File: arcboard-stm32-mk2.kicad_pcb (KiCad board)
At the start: 2 copper layers, 60 x 60 mm, 88 parts, among them J1 Conn_01x04_Socket, J17 Conn_01x04_Socket, J2 Conn_01x04_Socket, J3 Conn_01x04_Socket, J5 Conn_01x02_Socket, J6 Conn_01x02_Socket, J7 Conn_01x02_Socket, U1 XC6210B332MR-G, U13 2N7002, U14 W25Q128JVSIQTR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

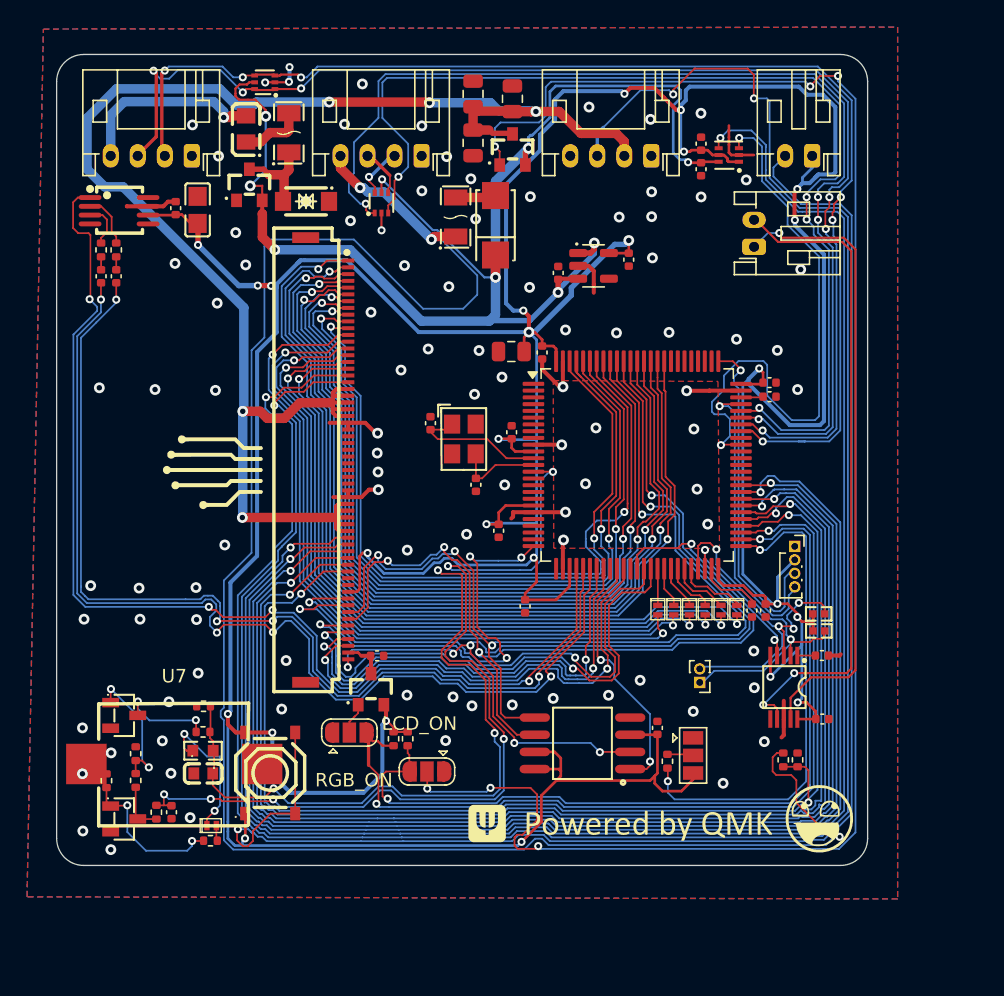
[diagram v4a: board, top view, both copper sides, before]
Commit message: re-organized the bottom section to fit a piezo
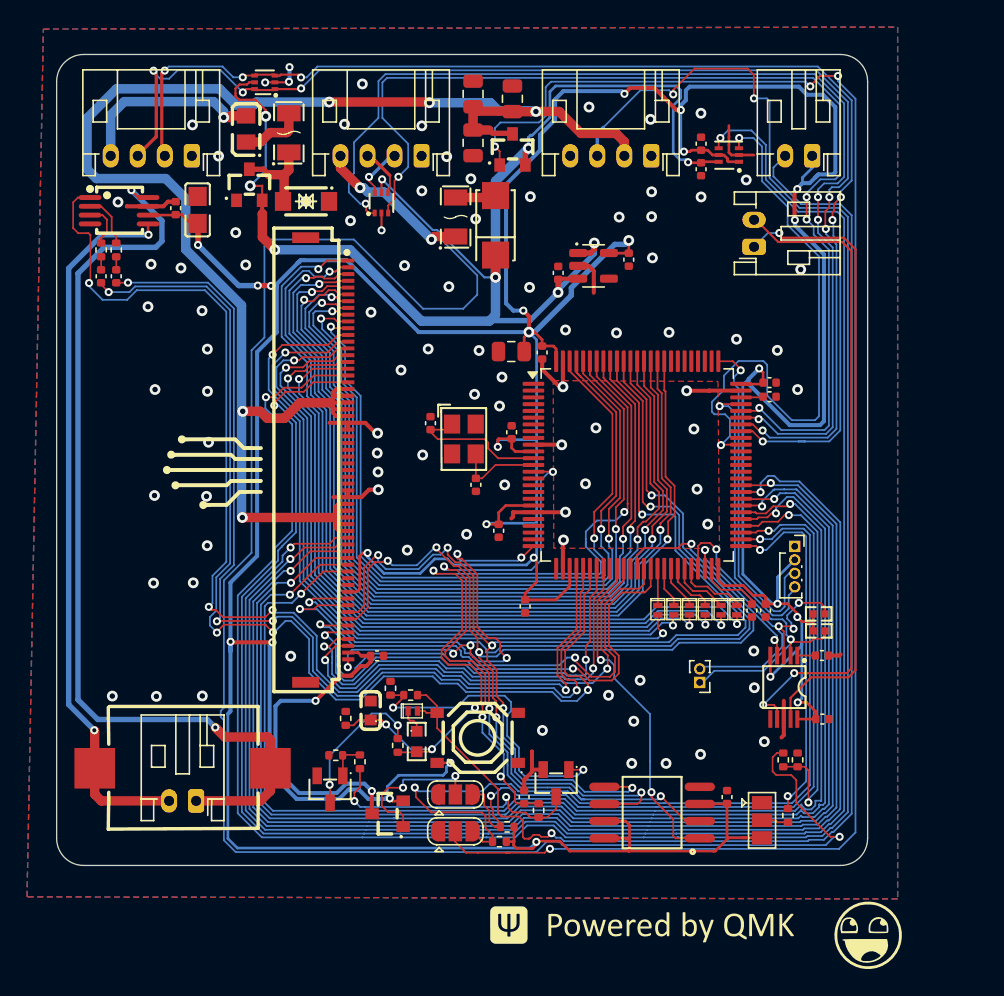
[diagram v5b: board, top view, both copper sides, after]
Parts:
- added J4: Conn_01x02_Socket, Connector_JST:JST_PH_S2B-PH-K_1x02_P2.00mm_Horizontal, F.Cu at (80.3, 125.2)
- moved U13 32.1 mm to (107.0, 123.9), turned to 90 degrees
- moved R14 28.3 mm to (105.7, 125.9)
- moved C17 26.1 mm to (104.6, 124.9), turned to -90 degrees
- moved R16 22.1 mm to (94.7, 116.9)
- moved R15 18.3 mm to (96.2, 117.4)
- moved D11 17.1 mm to (96.3, 118.6)
- moved R3 16.6 mm to (92.4, 122.3)
- moved U4 16.2 mm to (90.2, 124.4), turned to 90 degrees
- moved R6 15.8 mm to (96.6, 120.8), turned to -90 degrees
- moved U15 15.6 mm to (101.2, 120.6), turned to 180 degrees
- moved R9 14.8 mm to (90.7, 121.8), turned to 180 degrees
- moved R2 14.4 mm to (95.2, 121.1), turned to -90 degrees
- moved C22 13.2 mm to (93.2, 118.5), turned to 90 degrees
- moved R8 10.6 mm to (103.3, 127.2), turned to 180 degrees
- moved R1 10.6 mm to (91.4, 119.1), turned to 90 degrees
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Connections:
- U15 pad 1: +3V3 -> unconnected-(U15-A-Pad1)
- U15 pad 3: Net-(D11-A) -> unconnected-(U15-C-Pad3)
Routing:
- net VO-: track 0.00 -> 70.3 mm
- net VO+: track 0.00 -> 53.2 mm, vias 0 -> 2
- net NRST: track 65.4 -> 40.9 mm, vias 6 -> 4
- net LCD_3V3: track 3.09 -> 25.4 mm, vias 0 -> 2
- net BOOT0: track 82.2 -> 61.3 mm, vias 4 -> 5
- net Net-(D11-A): track 115.7 -> 95.2 mm
- net Net-(U13-D): track 3.87 -> 20.4 mm, vias 0 -> 2
- net SPI1_CLK: track 74.5 -> 89.6 mm, vias 4 -> 6
- net SPI1_MOSI: track 73.5 -> 87.4 mm, vias 4 -> 6
- net +3V3: track 371.8 -> 384.1 mm
- net Net-(U13-G): track 11.5 -> 23.3 mm
- net SPLIT_HAND: track 36.5 -> 26.5 mm
- net SPI1_MISO: track 75.4 -> 85.4 mm
- net LCD_ON: track 66.1 -> 56.5 mm
- net Net-(JP4-C): track 2.34 -> 11.2 mm, vias 0 -> 2
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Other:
- board text removed: "LCD_ON"
- board text removed: "RGB_ON"

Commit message: silkscreen work, adding lse crystal and vbat hookup
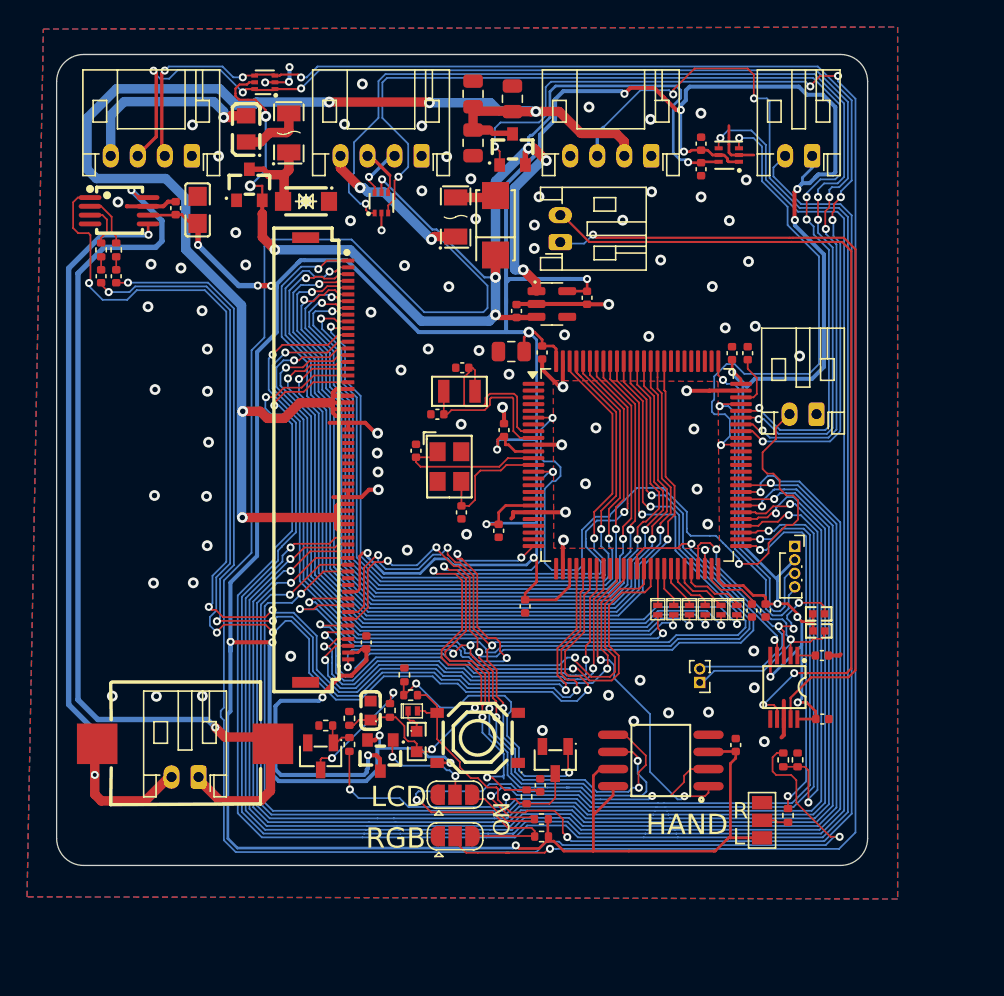
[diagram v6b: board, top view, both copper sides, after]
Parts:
- removed LOGO2: **REF, kicad-libraries:awesome-logo
- removed LOGO7: **REF, kicad-libraries:awesome-logo-25mm
- added C29: 12p, Capacitor_SMD:C_0402_1005Metric, F.Cu at (98.2, 96.6)
- added C30: 12p, Capacitor_SMD:C_0402_1005Metric, F.Cu at (100.0, 93.2)
- added J8: Conn_01x02_Socket, Connector_JST:JST_PH_S2B-PH-K_1x02_P2.00mm_Horizontal, F.Cu at (126.2, 96.6)
- added U8: SC-32S32_768kHz20PPM7pF, kicad-libraries:OSC-SMD_L3.2-W1.5, F.Cu at (99.8, 94.9)
- LOGO3, LOGO4: moved to B.Cu
- moved LOGO3 19.1 mm to (73.8, 83.2), turned to 180 degrees
- moved J7 14.3 mm to (107.3, 83.9)
- moved LOGO4 8.46 mm to (117.7, 127.2), turned to 180 degrees
- moved MOSFET3 4.33 mm to (94.0, 121.9), turned to 90 degrees
- moved C13 4.18 mm to (104.0, 89.0)
- moved C27 4.18 mm to (109.2, 88.0)
- moved U1 4.18 mm to (106.6, 88.5)
- moved U14 3.90 mm to (114.7, 122.2)
- moved C14 3.90 mm to (120.2, 121.1)
- moved C21 3.60 mm to (121.1, 92.1), turned to -90 degrees
- moved C7 3.53 mm to (120.0, 92.1), turned to -90 degrees
- moved R7 3.14 mm to (105.9, 127.9)
- moved R2 2.65 mm to (94.7, 118.5)
- moved R8 2.61 mm to (105.9, 126.6)
- moved U4 2.54 mm to (89.5, 121.9)
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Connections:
- U2 pad 6: unconnected-(U2-VBAT-Pad6) -> VBAT
- U2 pad 8: unconnected-(U2-PC14-Pad8) -> LSE_OSC32_IN
- U2 pad 9: unconnected-(U2-PC15-Pad9) -> LSE_OSC32_OUT
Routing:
- net VBAT: track 0.00 -> 52.8 mm, vias 0 -> 2
- net HAPTIC_pos: track 48.6 -> 63.1 mm
- net HAPTIC_neg: track 46.9 -> 61.0 mm
- net LSE_OSC32_IN: track 0.00 -> 13.2 mm
- net LSE_OSC32_OUT: track 0.00 -> 11.7 mm
- net LED_SIG_OUTPUT: track 43.4 -> 37.2 mm
- net +3V3: track 384.1 -> 378.0 mm, vias 25 -> 24
- net RGB_ON: track 65.2 -> 70.4 mm
- net SPI1_MOSI: track 87.4 -> 91.5 mm
- net VO+: track 53.2 -> 57.2 mm
- net Net-(JP4-C): track 11.2 -> 7.95 mm
- net LCD_ON: track 56.5 -> 59.5 mm
- net PH1: track 6.49 -> 9.44 mm
- net Net-(U2-VCAP_2): track 1.66 -> 4.09 mm
- net NRST: track 40.9 -> 42.9 mm
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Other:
- board text added: "HAND"
- board text added: "LCD"
- board text added: "ON"
- board text added: "R L"
- board text added: "RGB"

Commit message: fixing issues brought up by drashna, adding timer notation to schematic
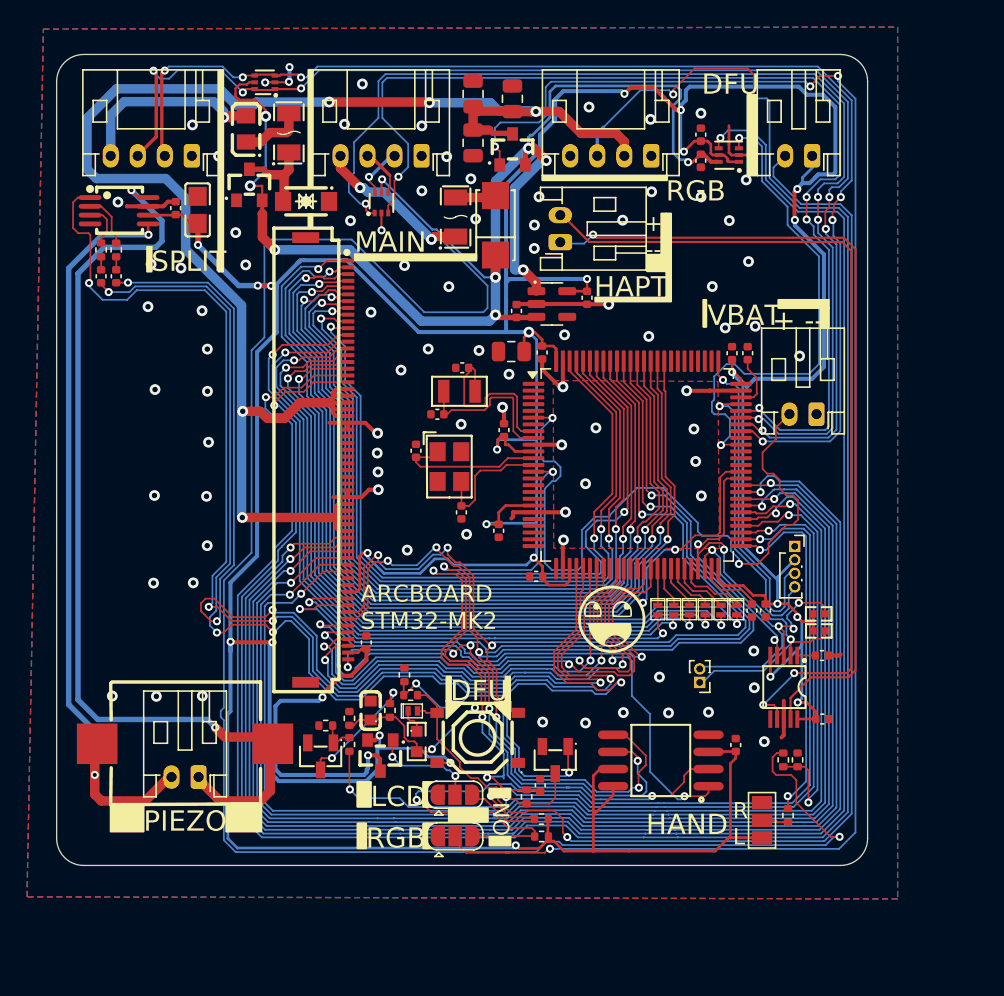
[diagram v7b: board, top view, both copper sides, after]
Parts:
- added LOGO1: **REF, kicad-libraries:awesome-logo, F.Cu at (111.1, 111.8)
- moved C11 2.37 mm to (105.5, 108.6), turned to 0 degrees
- moved C18 0.67 mm to (117.7, 75.9)
- moved C19 0.63 mm to (117.7, 77.9)
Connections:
- U2 pad 25: PMW_MOTION -> unconnected-(U2-PA2-Pad25)
- U2 pad 29: AMP_SD -> AMP_IN+
- U2 pad 31: AMP_IN+ -> AMP_SD
- U2 pad 38: HAPTIC_PWM -> unconnected-(U2-PE7-Pad38)
- U2 pad 61: unconnected-(U2-PD14-Pad61) -> HAPTIC_PWM
- U2 pad 62: unconnected-(U2-PD15-Pad62) -> PMW_MOTION
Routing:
- net PMW_MOTION: track 35.8 -> 52.3 mm
- net AMP_IN-: track 75.9 -> 83.1 mm
- net AMP_SD: track 84.7 -> 91.2 mm
- net AMP_IN+: track 80.4 -> 86.2 mm
- net +3V3: track 378.0 -> 375.8 mm
- net HAPTIC_PWM: track 16.5 -> 18.3 mm
- net LCD_BL: track 34.6 -> 36.2 mm
- net LCD_RST: track 39.6 -> 41.2 mm
- net PMW_CS: track 40.0 -> 41.1 mm
- net FLASH_CS: track 23.4 -> 24.1 mm
- net LCD_CS: track 33.6 -> 34.1 mm
- net GND: vias 89 -> 88
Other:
- board text added: "+ --"
- board text added: "ARCBOARD STM32-MK2"
- board text added: "DFU"
- board text added: "HAPT"
- board text added: "MAIN"
- board text added: "PIEZO"
- board text added: "SPLIT"
- board text added: "VBAT"

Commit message: improving top silkscreen
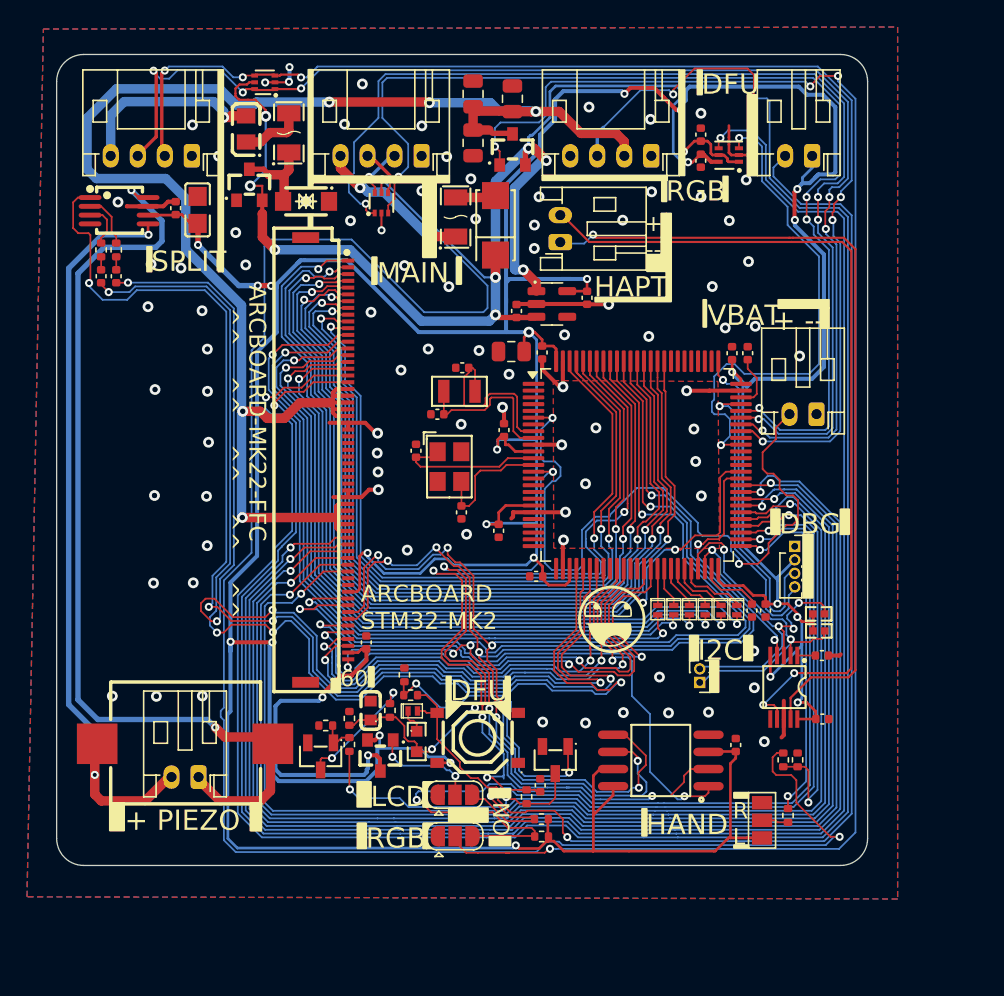
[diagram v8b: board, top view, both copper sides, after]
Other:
- board text added: "+ PIEZO -"
- board text added: "60"
- board text added: "ARCBOARD-MK22-FFC ^^ ^^ ^^ ^^ ^^"
- board text added: "DBG"
- board text added: "I2C"
- board text removed: "PIEZO"
